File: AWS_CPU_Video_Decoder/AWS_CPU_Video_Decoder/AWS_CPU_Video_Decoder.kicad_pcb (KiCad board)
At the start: 2 copper layers, 132 x 99.6 mm, 177 parts, among them J1 Conn_02x20_Odd_Even, J10 Conn_01x04_Pin, J11 Conn_01x04_Pin, J12 Conn_01x04_Pin, J13 Conn_01x04_Pin, J14 Conn_01x04_Pin, J15 Conn_01x04_Pin, J16 Video, J18 Conn_01x02_Pin, J19 Conn_01x02_Pin, J2 Conn_01x04_Pin, J3 Video, J4 Conn_01x04_Pin, J5 Conn_02x20_Odd_Even, J6 Conn_01x04_Pin, J7 Conn_01x04_Pin, J8 Conn_01x04_Pin, J9 Conn_01x04_Pin, SW1 Reset

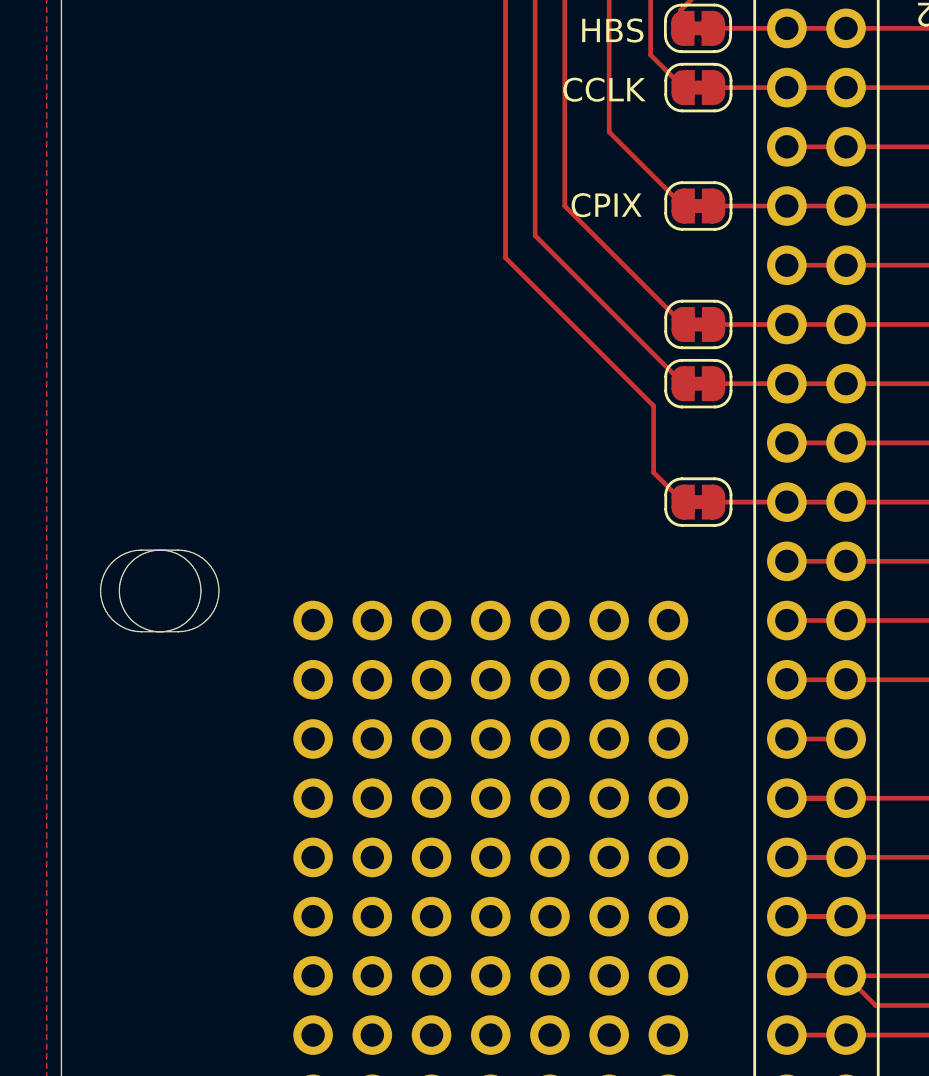
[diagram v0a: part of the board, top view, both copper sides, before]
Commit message: Added rotary encoder for switching mode and scrolling
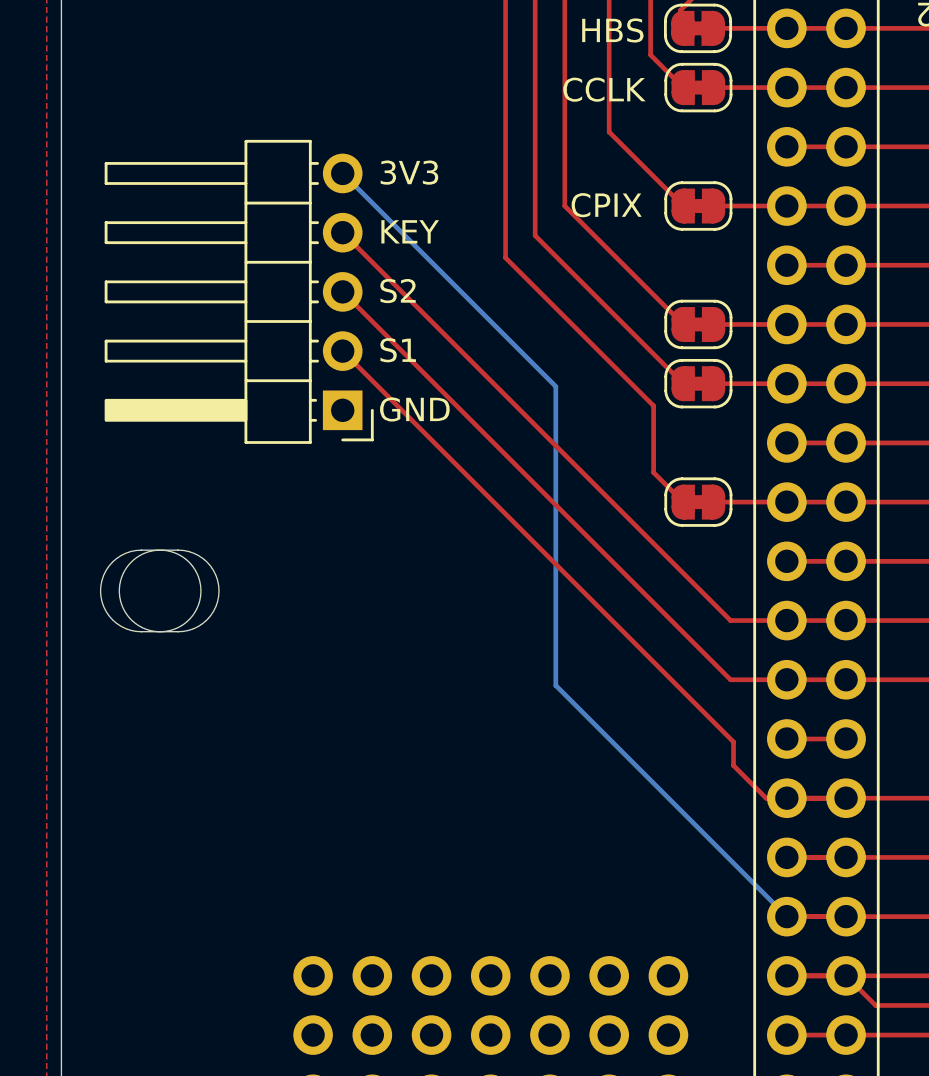
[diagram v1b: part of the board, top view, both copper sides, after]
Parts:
- removed the ? at (94.7, 97.4)
- removed the ? at (102.4, 110.1)
- removed the ? at (89.7, 99.9)
- removed the ? at (102.4, 97.4)
- removed the ? at (99.8, 105.0)
- removed the ? at (92.2, 107.6)
- removed the ? at (94.7, 107.6)
- removed the ? at (94.7, 102.5)
- removed the ? at (89.7, 97.4)
- removed the ? at (97.3, 107.6)
- removed the ? at (92.2, 99.9)
- removed the ? at (102.4, 99.9)
- removed the ? at (94.7, 110.1)
- removed the ? at (104.9, 102.5)
- removed the ? at (89.7, 102.5)
- removed the ? at (92.2, 110.1)
- removed the ? at (99.8, 107.6)
- removed the ? at (97.3, 102.5)
- removed the ? at (94.7, 99.9)
- removed the ? at (104.9, 105.0)
- removed the ? at (99.8, 99.9)
- removed the ? at (92.2, 102.5)
- removed the ? at (99.8, 97.4)
- removed the ? at (102.4, 102.5)
- removed the ? at (92.2, 105.0)
- removed the ? at (97.3, 105.0)
- removed the ? at (104.9, 99.9)
- removed the ? at (89.7, 107.6)
- removed the ? at (102.4, 105.0)
- removed the ? at (97.3, 99.9)
- removed the ? at (94.7, 105.0)
- removed the ? at (92.2, 97.4)
- removed the ? at (104.9, 110.1)
- removed the ? at (99.8, 102.5)
- removed the ? at (89.7, 110.1)
- removed the ? at (97.3, 97.4)
- removed the ? at (89.7, 105.0)
- removed the ? at (97.3, 110.1)
- removed the ? at (104.9, 97.4)
- removed the ? at (104.9, 107.6)
- removed the ? at (99.8, 110.1)
- removed the ? at (102.4, 107.6)
- added J20: Encoder, Connector_PinHeader_2.54mm:PinHeader_1x05_P2.54mm_Horizontal, F.Cu at (90.9, 88.4)
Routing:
- net +3V3: track 204.2 -> 244.0 mm
- net GPIO28: track 11.9 -> 39.5 mm
- net GPIO27: track 9.36 -> 35.3 mm
- net GPIO26: track 9.36 -> 35.3 mm
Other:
- board text added: "3V3"
- board text added: "KEY"
- board text added: "S1"
- board text added: "S2"
